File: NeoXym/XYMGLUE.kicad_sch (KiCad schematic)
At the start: 48 parts, among them J1 Conn_01x08, J2 Conn_01x08, SW1 SW_Push, SW2 SW_Push, SW3 SW_SPDT, SW4 SW_SPDT, SW5 SW_Push, U1 74HCT138, U10 74AHCT04, U15 74HCT00, U16 74HCT14, U17 74HCT121, U18 NE555P, U19 MAX232, U2 74HCT138, U4 74HCT32, U5 74HCT00, U6 74HCT09, U8 74LS10, U9 74HCT00, X1 1.8432MHz

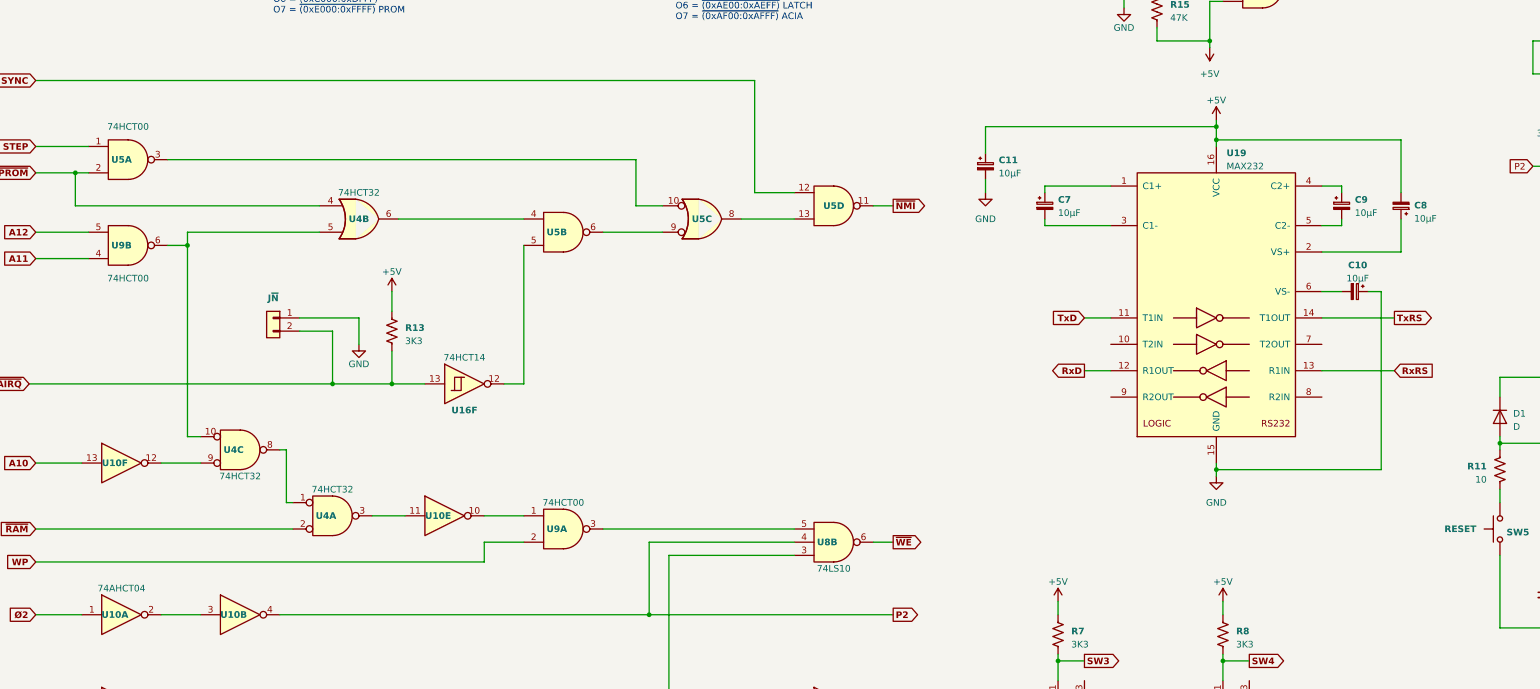
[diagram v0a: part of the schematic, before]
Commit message: modified:   NeoXym/CPU_MEM_IOCTRL.kicad_sch 	modified:   NeoXym/XYMGLUE.kicad_sch 	modified:   NeoXym/XYMPOWER.kicad_sch
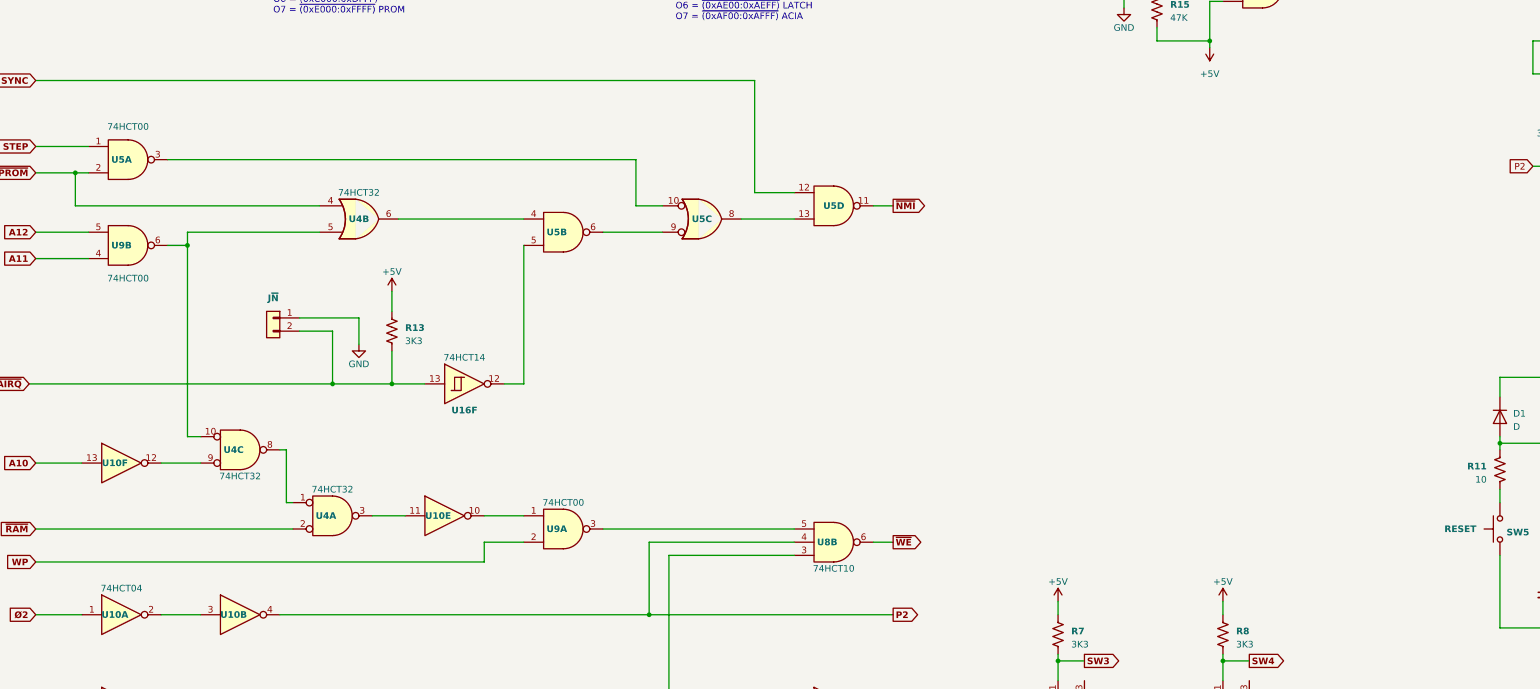
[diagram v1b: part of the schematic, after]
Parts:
- removed C10, C11, C7, C8, C9: 10µF, symbol Device:C_Polarized_Small
- removed U19: MAX232, symbol Interface_UART:MAX232
- U10: value 74AHCT04 -> 74HCT04
- U8: value 74LS10 -> 74HCT10

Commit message: modified:   CPU_MEM_IOCTRL.kicad_sch 	modified:   XYMGLUE.kicad_sch 	modified:   XYMPOWER.kicad_sch
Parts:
- added J13: Conn_01x08, symbol Connector_Generic:Conn_01x08
- added U23: 74HCT138, symbol 74xx:74LS138
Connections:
- net +5V: now also U23.16 (VCC), U23.6 (E3)
- net GND: now also U23.8 (GND)
- net ~{ACIA}: now also U23.4 (E1)
- new net ADDR4: U23.1 (A0)
- new net ADDR5: U23.2 (A1)
- new net ADDR6: U23.3 (A2)
- new net ADDR7: U23.5 (E2)
- new net ~{ACIA0}: J13.1 (Pin_1), U23.15 (O0)
- new net ~{ACIA1}: J13.2 (Pin_2), U23.14 (O1)
- new net ~{ACIA2}: J13.3 (Pin_3), U23.13 (O2)
- new net ~{ACIA3}: J13.4 (Pin_4), U23.12 (O3)
- new net ~{ACIA4}: J13.5 (Pin_5), U23.11 (O4)
- new net ~{ACIA5}: J13.6 (Pin_6), U23.10 (O5)
- new net ~{ACIA6}: J13.7 (Pin_7), U23.9 (O6)
- new net ~{ACIA7}: J13.8 (Pin_8), U23.7 (O7)
